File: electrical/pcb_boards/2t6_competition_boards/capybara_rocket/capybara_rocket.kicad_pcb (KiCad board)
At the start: 4 copper layers, 160 x 65 mm, 95 parts, among them J1 3.6V Battery, J10 Elevator, J11 SparkFun MAX-M10S, J12 Aileron 1, J13 Aileron 2, J14 Ground Camera, J15 Payload Camera, J16 DC Motor, J2 1.2V Battery, J3 3.6V Switch, J4 1.2V Switch, J5 LED, J6 NC, J7 CC, J8 VL53L1-SATEL, J9 Egg, Q1 SI4435DDY, U1 DS1307+, U10 MP3414, U11 SN74LVC1G04, U12 MCP1640, U13 EEPROM, U14 STM32 NUCLEO-G431KB, U15 SparkFun XBee Explorer, U2 Adafruit BNO085, U3 TLC555, U4 LTC3536, U5 LTC3536, U6 Adafruit BMP581, U7 DRV8212DRLR, U8 INA219, U9 TPS3839, Y1 AB38T-32.768KHZ

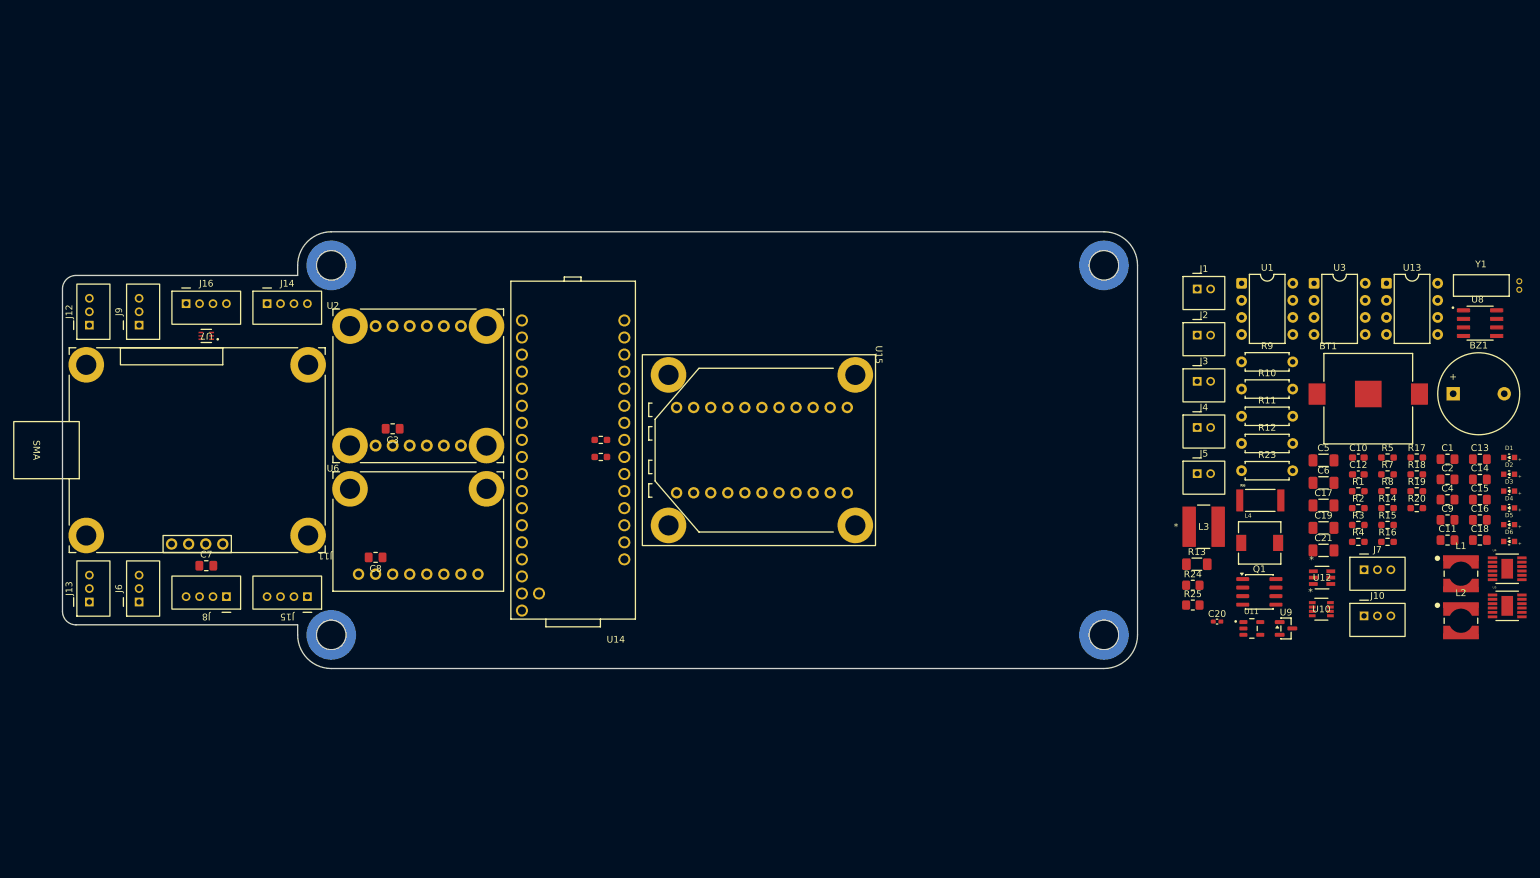
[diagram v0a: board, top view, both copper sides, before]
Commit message: Finalized schematic design for CPL and ERC pass
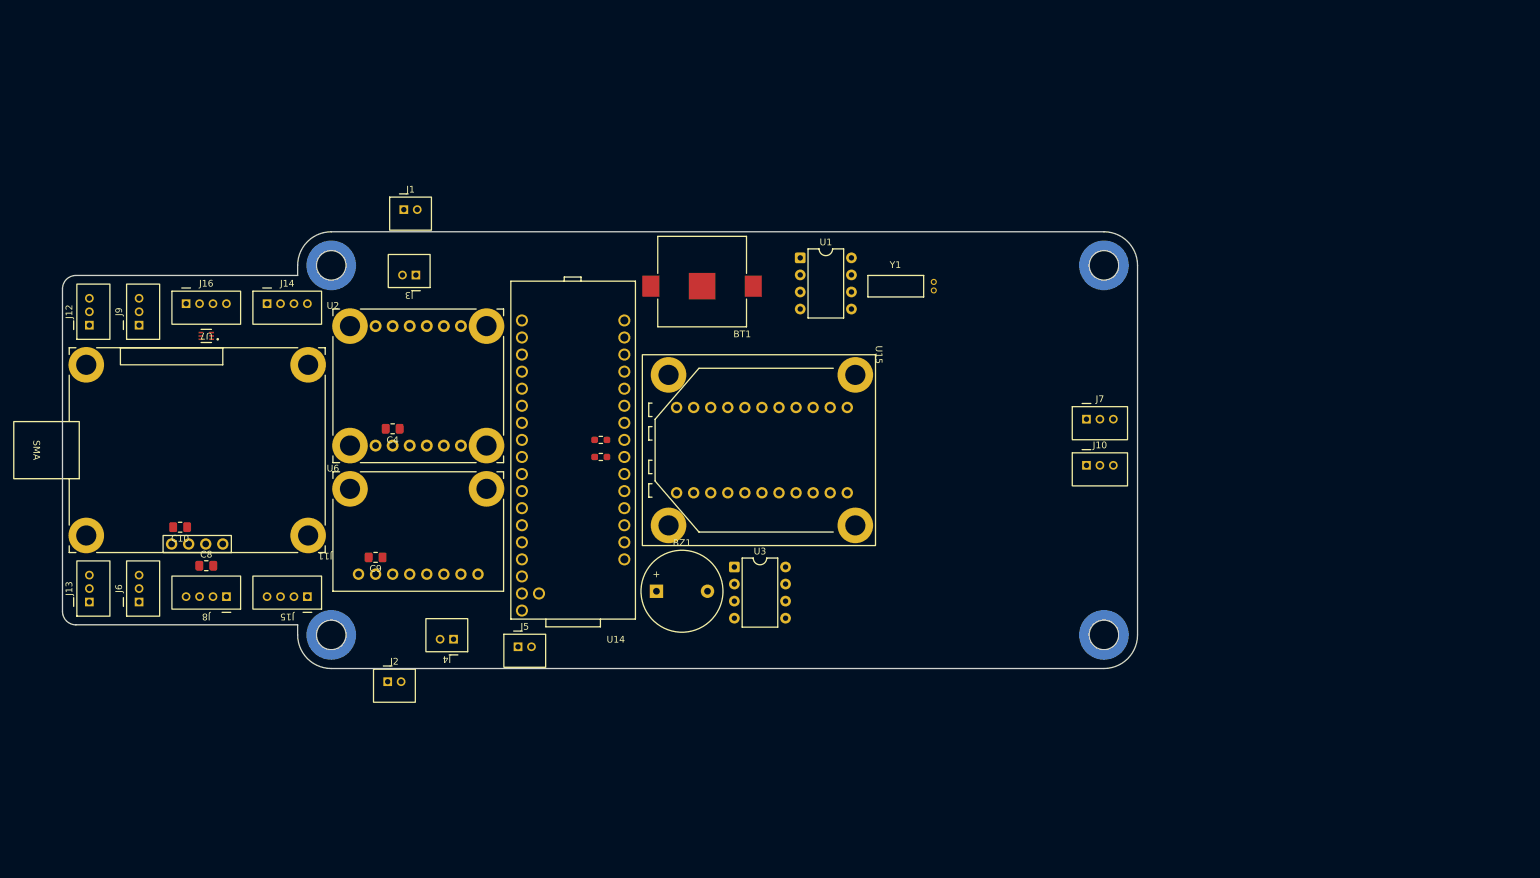
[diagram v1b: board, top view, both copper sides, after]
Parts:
- removed C1: 20μF, Capacitor_SMD:C_0805_2012Metric_Pad1.18x1.45mm_HandSolder
- removed C11, C13: 220pF, Capacitor_SMD:C_0805_2012Metric_Pad1.18x1.45mm_HandSolder
- removed C12: 47pF, Capacitor_SMD:C_0603_1608Metric_Pad1.08x0.95mm_HandSolder
- removed C14, C2: 0.1μF, Capacitor_SMD:C_0805_2012Metric_Pad1.18x1.45mm_HandSolder
- removed C15, C16, C18: 22μF, Capacitor_SMD:C_0805_2012Metric_Pad1.18x1.45mm_HandSolder
- removed C17, C19, C21, C5, C6: 10μF, Capacitor_SMD:C_1206_3216Metric_Pad1.33x1.80mm_HandSolder
- removed C20: 1μF, Capacitor_SMD:C_0402_1005Metric_Pad0.74x0.62mm_HandSolder
- removed the C4 at (276.1, 107.4)
- removed the C9 at (276.1, 110.4)
- removed D1, D2, D3, D4, D5, D6: LED, DigiKey:WL-SMCW_0603
- removed L1, L2: 15μH, RSX_CanSat_Custom_KiCad_Footprints:WE-TPC_4828
- removed L3: 2.2μH, RSX_CanSat_Custom_KiCad_Footprints:IND_BOURNS_SRN6045
- removed L4: 4.7μH, RSX_CanSat_Custom_KiCad_Footprints:IND_B82462G4472M000
- removed Q1: SI4435DDY, Package_SO:SOIC-8_3.9x4.9mm_P1.27mm
- removed R1: 100kΩ, Resistor_SMD:R_0603_1608Metric_Pad0.98x0.95mm_HandSolder
- removed R10, R9: 221kΩ, Resistor_THT:R_Axial_DIN0207_L6.3mm_D2.5mm_P7.62mm_Horizontal
- removed R11, R12: 1MΩ, Resistor_THT:R_Axial_DIN0207_L6.3mm_D2.5mm_P7.62mm_Horizontal
- removed R13: 61.9kΩ, Resistor_SMD:R_1206_3216Metric_Pad1.30x1.75mm_HandSolder
- removed R14, R15, R16, R17, R18, R19: 100Ω, Resistor_SMD:R_0603_1608Metric_Pad0.98x0.95mm_HandSolder
- removed R2: 5.1kΩ, Resistor_SMD:R_0603_1608Metric_Pad0.98x0.95mm_HandSolder
- removed R20: 505kΩ, Resistor_SMD:R_0603_1608Metric_Pad0.98x0.95mm_HandSolder
- removed R23: 100kΩ, Resistor_THT:R_Axial_DIN0207_L6.3mm_D2.5mm_P7.62mm_Horizontal
- removed R24: 976kΩ, Resistor_SMD:R_0805_2012Metric_Pad1.20x1.40mm_HandSolder
- removed R25: 562kΩ, Resistor_SMD:R_0805_2012Metric_Pad1.20x1.40mm_HandSolder
- removed R3: 10Ω, Resistor_SMD:R_0603_1608Metric_Pad0.98x0.95mm_HandSolder
- removed R4, R5: 51kΩ, Resistor_SMD:R_0603_1608Metric_Pad0.98x0.95mm_HandSolder
- removed R6: PT2512FK-070R1L, RSX_CanSat_Custom_KiCad_Footprints:RESC6331X65N
- removed R7, R8: 6.2kΩ, Resistor_SMD:R_0603_1608Metric_Pad0.98x0.95mm_HandSolder
- removed U10: MP3414, RSX_CanSat_Custom_KiCad_Footprints:TSOT23-8_MP3414A
- removed U11: SN74LVC1G04, RSX_CanSat_Custom_KiCad_Footprints:SOT95P280X145-5N
- removed U12: MCP1640, RSX_CanSat_Custom_KiCad_Footprints:SOT-23-6_MC_MCH
- removed U13: EEPROM, Package_DIP:DIP-8_W7.62mm
- removed U4, U5: LTC3536, RSX_CanSat_Custom_KiCad_Footprints:MSOP-12_MSE
- removed U8: INA219, RSX_CanSat_Custom_KiCad_Footprints:SOIC127P599X175-8N
- removed U9: TPS3839, Package_TO_SOT_SMD:SOT-23
- C10: value 47pF -> 0.1μF; footprint Capacitor_SMD:C_0603_1608Metric_Pad1.08x0.95mm_HandSolder -> Capacitor_SMD:C_0805_2012Metric_Pad1.18x1.45mm_HandSolder
- moved C10 175.7 mm to (87.5, 111.5), turned to 180 degrees
- moved J2 131.1 mm to (118.4, 134.5)
- moved BZ1 122.2 mm to (158.4, 121.0)
- moved J1 118.7 mm to (120.8, 64.2)
- moved J3 117.3 mm to (122.6, 73.9), turned to 180 degrees
- moved J4 115.1 mm to (128.2, 128.1), turned to 180 degrees
- moved J5 104.3 mm to (137.8, 129.3)
- moved BT1 100.4 mm to (165.2, 75.6), turned to 180 degrees
- moved U3 96.1 mm to (170.0, 117.4)
- moved Y1 87.1 mm to (199.7, 75.6)
- moved U1 65.8 mm to (179.8, 71.4)
- moved J7 47.0 mm to (222.4, 95.4)
- moved J10 47.0 mm to (222.4, 102.3)
- renumbered C3 to C4, C7 to C8, C8 to C9
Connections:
- net 1.2V renamed 1.2V B
- net 3.6V+ renamed 3.6V B
- C10 pad 1: Net-(C10-Pad1) -> 3.3V
- C10 pad 2: 3.3V -> GND
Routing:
- added copper zone on In1.Cu, net GND

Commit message: New graphics and layout work
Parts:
- added C1: 10μF, Capacitor_SMD:C_1206_3216Metric_Pad1.33x1.80mm_HandSolder, F.Cu at (122.0, 124.2)
- added C11: 47pF, Capacitor_SMD:C_0603_1608Metric_Pad1.08x0.95mm_HandSolder, F.Cu at (194.9, 36.6)
- added C12: 220pF, Capacitor_SMD:C_0805_2012Metric_Pad1.18x1.45mm_HandSolder, F.Cu at (199.6, 35.8)
- added C13: 47pF, Capacitor_SMD:C_0603_1608Metric_Pad1.08x0.95mm_HandSolder, F.Cu at (242.3, 51.8)
- added C14: 220pF, Capacitor_SMD:C_0805_2012Metric_Pad1.18x1.45mm_HandSolder, F.Cu at (244.6, 55.2)
- added C15: 0.1μF, Capacitor_SMD:C_0805_2012Metric_Pad1.18x1.45mm_HandSolder, F.Cu at (150.5, 151.8)
- added C16: 22μF, Capacitor_SMD:C_0805_2012Metric_Pad1.18x1.45mm_HandSolder, F.Cu at (199.6, 39.6)
- added C17: 22μF, Capacitor_SMD:C_0805_2012Metric_Pad1.18x1.45mm_HandSolder, F.Cu at (246.6, 52.0)
- added C18: 10μF, Capacitor_SMD:C_1206_3216Metric_Pad1.33x1.80mm_HandSolder, F.Cu at (260.2, 147.8)
- added C19: 22μF, Capacitor_SMD:C_0805_2012Metric_Pad1.18x1.45mm_HandSolder, F.Cu at (264.6, 144.0)
- added C2: 0.1μF, Capacitor_SMD:C_0805_2012Metric_Pad1.18x1.45mm_HandSolder, F.Cu at (138.0, 70.8)
- added C20: 10μF, Capacitor_SMD:C_1206_3216Metric_Pad1.33x1.80mm_HandSolder, F.Cu at (195.6, 143.0)
- added C21: 1μF, Capacitor_SMD:C_0402_1005Metric_Pad0.74x0.62mm_HandSolder, F.Cu at (261.6, 141.4)
- added C22: 10μF, Capacitor_SMD:C_1206_3216Metric_Pad1.33x1.80mm_HandSolder, F.Cu at (201.0, 140.6)
- added C3: 10μF, Capacitor_SMD:C_1206_3216Metric_Pad1.33x1.80mm_HandSolder, F.Cu at (122.0, 129.4)
- added C5: 10μF, Capacitor_SMD:C_1206_3216Metric_Pad1.33x1.80mm_HandSolder, F.Cu at (137.6, 129.4)
- added C6: 10μF, Capacitor_SMD:C_1206_3216Metric_Pad1.33x1.80mm_HandSolder, F.Cu at (189.2, 50.2)
- added C7: 10μF, Capacitor_SMD:C_1206_3216Metric_Pad1.33x1.80mm_HandSolder, F.Cu at (246.2, 47.6)
- added D1: LED, DigiKey:WL-SMCW_0603, F.Cu at (225.0, 112.8)
- added D2: LED, DigiKey:WL-SMCW_0603, F.Cu at (225.0, 106.8)
- added D3: LED, DigiKey:WL-SMCW_0603, F.Cu at (225.0, 100.8)
- added D4: LED, DigiKey:WL-SMCW_0603, F.Cu at (225.0, 94.8)
- added D5: LED, DigiKey:WL-SMCW_0603, F.Cu at (225.0, 88.8)
- added D6: LED, DigiKey:WL-SMCW_0603, F.Cu at (225.0, 109.8)
- added D7: LED, DigiKey:WL-SMCW_0603, F.Cu at (225.0, 103.8)
- added D8: LED, DigiKey:WL-SMCW_0603, F.Cu at (225.0, 97.8)
- added D9: LED, DigiKey:WL-SMCW_0603, F.Cu at (225.0, 91.8)
- added G***: LOGO, CAN-RGX:canada, F.Cu at (146.0, 129.6)
- added G***: LOGO, RSX_CanSat_Graphics:rsx_new_logo, F.Cu at (147.4, 136.2)
- added G***: LOGO, RSX_CanSat_Graphics:payload_2t6_drawing, B.Cu at (99.4, 111.8)
- added G***: LOGO, CAN-RGX:canada, B.Cu at (74.2, 105.6)
- added G***: LOGO, CAN-RGX:uoft, B.Cu at (105.6, 100.0)
- added G***: LOGO, RSX_CanSat_Graphics:rsx_new_logo, B.Cu at (74.2, 94.6)
- added G***: LOGO, RSX_CanSat_Graphics:cansat_logo_2, B.Cu at (91.6, 89.2)
- added L1: 15μH, RSX_CanSat_Custom_KiCad_Footprints:WE-TPC_4828, F.Cu at (188.8, 43.9)
- added L2: 15μH, RSX_CanSat_Custom_KiCad_Footprints:WE-TPC_4828, F.Cu at (239.6, 45.3)
- added L3: 2.2μH, RSX_CanSat_Custom_KiCad_Footprints:IND_BOURNS_SRN6045, F.Cu at (246.2, 149.0)
- added L4: 4.7μH, RSX_CanSat_Custom_KiCad_Footprints:IND_B82462G4472M000, F.Cu at (210.2, 148.6)
- added Q1: SI4435DDY, Package_SO:SOIC-8_3.9x4.9mm_P1.27mm, F.Cu at (245.9, 77.5)
- added Q2: SI4435DDY, Package_SO:SOIC-8_3.9x4.9mm_P1.27mm, F.Cu at (186.7, 152.9)
- added R1: 100kΩ, Resistor_SMD:R_0603_1608Metric_Pad0.98x0.95mm_HandSolder, F.Cu at (124.3, 123.9)
- added R10: 221kΩ, Resistor_THT:R_Axial_DIN0207_L6.3mm_D2.5mm_P7.62mm_Horizontal, F.Cu at (250.8, 51.6)
- added R11: 1MΩ, Resistor_THT:R_Axial_DIN0207_L6.3mm_D2.5mm_P7.62mm_Horizontal, F.Cu at (201.2, 54.9)
- added R12: 1MΩ, Resistor_THT:R_Axial_DIN0207_L6.3mm_D2.5mm_P7.62mm_Horizontal, F.Cu at (250.8, 55.5)
- added R13: 61.9kΩ, Resistor_SMD:R_1206_3216Metric_Pad1.30x1.75mm_HandSolder, F.Cu at (254.0, 148.2)
- added R14: 100Ω, Resistor_SMD:R_0603_1608Metric_Pad0.98x0.95mm_HandSolder, F.Cu at (225.0, 114.2)
- added R15: 100Ω, Resistor_SMD:R_0603_1608Metric_Pad0.98x0.95mm_HandSolder, F.Cu at (225.0, 108.2)
- added R16: 100Ω, Resistor_SMD:R_0603_1608Metric_Pad0.98x0.95mm_HandSolder, F.Cu at (225.0, 102.2)
- added R17: 100Ω, Resistor_SMD:R_0603_1608Metric_Pad0.98x0.95mm_HandSolder, F.Cu at (225.0, 96.2)
- added R18: 100Ω, Resistor_SMD:R_0603_1608Metric_Pad0.98x0.95mm_HandSolder, F.Cu at (225.0, 90.2)
- added R19: 100Ω, Resistor_SMD:R_0603_1608Metric_Pad0.98x0.95mm_HandSolder, F.Cu at (225.0, 111.2)
- added R2: 5.1kΩ, Resistor_SMD:R_0603_1608Metric_Pad0.98x0.95mm_HandSolder, F.Cu at (124.3, 127.5)
- added R20: 100Ω, Resistor_SMD:R_0603_1608Metric_Pad0.98x0.95mm_HandSolder, F.Cu at (225.0, 105.2)
- added R21: 100Ω, Resistor_SMD:R_0603_1608Metric_Pad0.98x0.95mm_HandSolder, F.Cu at (225.0, 99.2)
- added R22: 100Ω, Resistor_SMD:R_0603_1608Metric_Pad0.98x0.95mm_HandSolder, F.Cu at (225.0, 93.2)
- added R23: 505kΩ, Resistor_SMD:R_0603_1608Metric_Pad0.98x0.95mm_HandSolder, F.Cu at (257.5, 144.2)
- added R26: 976kΩ, Resistor_SMD:R_0805_2012Metric_Pad1.20x1.40mm_HandSolder, F.Cu at (206.6, 139.1)
- added R27: 562kΩ, Resistor_SMD:R_0805_2012Metric_Pad1.20x1.40mm_HandSolder, F.Cu at (206.6, 142.0)
- added R3: 10Ω, Resistor_SMD:R_0603_1608Metric_Pad0.98x0.95mm_HandSolder, F.Cu at (116.8, 123.0)
- added R4: 51kΩ, Resistor_SMD:R_0603_1608Metric_Pad0.98x0.95mm_HandSolder, F.Cu at (195.4, 50.2)
- added R5: 51kΩ, Resistor_SMD:R_0603_1608Metric_Pad0.98x0.95mm_HandSolder, F.Cu at (251.9, 43.0)
- added R6: PT2512FK-070R1L, RSX_CanSat_Custom_KiCad_Footprints:RESC6331X65N, F.Cu at (144.2, 148.9)
- added R7: 6.2kΩ, Resistor_SMD:R_0603_1608Metric_Pad0.98x0.95mm_HandSolder, F.Cu at (199.3, 50.6)
- added R8: 6.2kΩ, Resistor_SMD:R_0603_1608Metric_Pad0.98x0.95mm_HandSolder, F.Cu at (251.5, 47.4)
- added R9: 221kΩ, Resistor_THT:R_Axial_DIN0207_L6.3mm_D2.5mm_P7.62mm_Horizontal, F.Cu at (201.2, 46.8)
- added TP1: TestPoint, TestPoint:TestPoint_THTPad_2.0x2.0mm_Drill1.0mm, F.Cu at (228.2, 113.5)
- added TP10: TestPoint, TestPoint:TestPoint_THTPad_2.0x2.0mm_Drill1.0mm, F.Cu at (228.2, 86.5)
- added TP2: TestPoint, TestPoint:TestPoint_THTPad_2.0x2.0mm_Drill1.0mm, F.Cu at (228.2, 107.5)
- added TP3: TestPoint, TestPoint:TestPoint_THTPad_2.0x2.0mm_Drill1.0mm, F.Cu at (228.2, 101.5)
- added TP4: TestPoint, TestPoint:TestPoint_THTPad_2.0x2.0mm_Drill1.0mm, F.Cu at (228.2, 95.5)
- added TP5: TestPoint, TestPoint:TestPoint_THTPad_2.0x2.0mm_Drill1.0mm, F.Cu at (228.2, 89.5)
- added TP6: TestPoint, TestPoint:TestPoint_THTPad_2.0x2.0mm_Drill1.0mm, F.Cu at (228.2, 110.5)
- added TP7: TestPoint, TestPoint:TestPoint_THTPad_2.0x2.0mm_Drill1.0mm, F.Cu at (228.2, 104.5)
- added TP8: TestPoint, TestPoint:TestPoint_THTPad_2.0x2.0mm_Drill1.0mm, F.Cu at (228.2, 98.5)
- added TP9: TestPoint, TestPoint:TestPoint_THTPad_2.0x2.0mm_Drill1.0mm, F.Cu at (228.2, 92.5)
- added U10: TPS3839, Package_TO_SOT_SMD:SOT-23-3, F.Cu at (248.3, 83.3)
- added U11: MP3414, RSX_CanSat_Custom_KiCad_Footprints:TSOT23-8_MP3414A, F.Cu at (250.8, 142.4)
- added U12: SN74LVC1G04, Package_TO_SOT_SMD:SOT-23-5, F.Cu at (243.5, 83.7)
- added U13: MCP1640, RSX_CanSat_Custom_KiCad_Footprints:SOT-23-6_MC_MCH, F.Cu at (202.5, 146.0)
- added U14: TPS3839, Package_TO_SOT_SMD:SOT-23-3, F.Cu at (189.3, 160.1)
- added U16: SN74AUP1G04, Package_TO_SOT_SMD:SOT-23-5, F.Cu at (183.7, 159.4)
- added U4: EEPROM, Package_DIP:DIP-8_W7.62mm, F.Cu at (122.1, 69.4)
- added U5: LTC3536, RSX_CanSat_Custom_KiCad_Footprints:MSOP-12_MSE, F.Cu at (196.0, 45.9)
- added U6: LTC3536, RSX_CanSat_Custom_KiCad_Footprints:MSOP-12_MSE, F.Cu at (246.5, 43.1)
- added U9: INA219, Package_SO:SOIC-8_3.9x4.9mm_P1.27mm, F.Cu at (150.5, 147.8)
- U8: renamed from U7; value DRV8212DRLR -> DRV8212
- moved Y1 56.3 mm to (143.6, 70.4), turned to 180 degrees
- moved U1 45.8 mm to (134.0, 69.4), turned to -90 degrees
- moved U3 45.1 mm to (126.9, 130.6), turned to 90 degrees
- moved J10 25.7 mm to (196.7, 102.8), turned to -90 degrees
- moved J7 25.5 mm to (197.1, 91.8), turned to -90 degrees
- moved J5 21.8 mm to (116.0, 128.8), turned to 90 degrees
- moved J4 21.1 mm to (116.6, 145.8), turned to 0 degrees
- moved J3 14.9 mm to (134.2, 64.5)
- moved C8 12.3 mm to (103.7, 117.2)
- moved J15 12.0 mm to (94.4, 121.8)
- moved J8 12.0 mm to (106.5, 121.8)
- moved J1 9.03 mm to (127.6, 58.3)
- moved J2 5.31 mm to (116.6, 139.5)
- moved BT1 1.84 mm to (165.6, 77.4)
- renumbered R21 to R24, R22 to R25, U14 to U15, U15 to U17, U6 to U7
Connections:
- J8 pad 2: SDA -> SCL
- J8 pad 3: SCL -> SDA
- U2 pad JP1_4: SCLK -> SCL
- U2 pad JP1_5: MISO -> SDA
- U2 pad JP2_5: MOSI -> unconnected-(U2-DI-PadJP2_5)
- U2 pad JP2_6: CS -> unconnected-(U2-CS-PadJP2_6)
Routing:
- net XBEE_TX: track 0.00 -> 19.5 mm
- net XBEE_RX: track 0.00 -> 15.9 mm
- net GND: track 0.00 -> 9.00 mm, vias 0 -> 9
- net Net-(D9-A): track 0.00 -> 2.33 mm
- net Net-(D8-A): track 0.00 -> 2.33 mm
- net Net-(D7-A): track 0.00 -> 2.33 mm
- net Net-(D6-A): track 0.00 -> 2.33 mm
- net Net-(D5-A): track 0.00 -> 2.33 mm
- net Net-(D4-A): track 0.00 -> 2.33 mm
- net Net-(D3-A): track 0.00 -> 2.33 mm
- net Net-(D2-A): track 0.00 -> 2.33 mm
- net Net-(D1-A): track 0.00 -> 2.33 mm
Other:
- board text added: "+ 3.6V"
- board text added: "- 3.6V"
- board text added: "1.2V"
- board text added: "100Ω"
- board text added: "3.3V"
- board text added: "5.5V"
- board text added: "AILERON"
- board text added: "Adam Kabbara Arthur Goetzke-Coburn Daniel Yu Luke Watson Angelique Liao Ada Selcuk Yulin Lin Jingshu Zhu Vincent Jia Wareesha Qureshi Parth Bhasin John Yfantis Nathan Xia Gianluca Ceccacci Berk Yilmaz Remi Zhang"
- board text added: "B 1.2V"
- board text added: "B 3.6V"
- board text added: "BZ 3.3V"
- board text added: "Designed by Daniel Yu & Adam Kabbara"
- board text added: "EGG"
- board text added: "GND"
- board text added: "G_IN"
- board text added: "G_OUT"
- board text added: "LED"
- board text added: "MCU 3.3V"
- board text added: "NC_REL"
- board text added: "PWM_1"
- board text added: "PWM_2"
- board text added: "P_IN"
- board text added: "P_OUT"
- board text added: "RSX Aerial CanSat 2T5-2T6"
- board text added: "SCL"
- board text added: "SDA"
